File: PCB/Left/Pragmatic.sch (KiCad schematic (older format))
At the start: 75 parts, among them J1 Conn_02x07_Odd_Even, SW1 SW_Push, SW10 SW_Push, SW11 SW_Push, SW12 SW_Push, SW13 SW_Push, SW14 SW_Push, SW15 SW_Push, SW16 SW_Push, SW17 SW_Push, SW18 SW_Push, SW19 SW_Push, SW2 SW_Push, SW20 SW_Push, SW21 SW_Push, SW22 SW_Push, SW23 SW_Push, SW24 SW_Push, SW25 SW_Push, SW26 SW_Push, SW27 SW_Push, SW28 SW_Push, SW29 SW_Push, SW3 SW_Push, SW30 SW_Push, SW31 SW_Push, SW32 SW_Push, SW33 SW_Push, SW34 SW_Push, SW35 SW_Push, SW36 SW_Push, SW4 SW_Push, SW5 SW_Push, SW6 SW_Push, SW7 SW_Push, SW8 SW_Push, SW9 SW_Push

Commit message: left ready
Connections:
- net Col1: now also J1.9 (Pin_9); no longer J1.6 (Pin_6)
- net Col2: now also J1.10 (Pin_10); no longer J1.8 (Pin_8)
- net Col3: now also J1.11 (Pin_11); no longer J1.10 (Pin_10)
- net Col5: now also J1.13 (Pin_13); no longer J1.14 (Pin_14)
- net Col6: now also J1.14 (Pin_14); no longer J1.13 (Pin_13)
- net Row4: now also J1.6 (Pin_6); no longer J1.11 (Pin_11)
- net Row5: now also J1.7 (Pin_7); no longer J1.9 (Pin_9)
- net Row6: now also J1.8 (Pin_8); no longer J1.7 (Pin_7)
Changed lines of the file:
@@
 Text GLabel 6070 2590 2    50   Input ~ 0
 Ground
-Text GLabel 6070 2790 2    50   Input ~ 0
+Text GLabel 5570 2990 0    50   Input ~ 0
 Col1
-Text GLabel 6070 2890 2    50   Input ~ 0
+Text GLabel 6070 2990 2    50   Input ~ 0
 Col2
+Text GLabel 6070 3190 2    50   Input ~ 0
+Col6
 Text GLabel 5570 3190 0    50   Input ~ 0
-Col6
-Text GLabel 6070 3190 2    50   Input ~ 0
 Col5
 Text GLabel 6070 3090 2    50   Input ~ 0
 Col4
-Text GLabel 6070 2990 2    50   Input ~ 0
+Text GLabel 5570 3090 0    50   Input ~ 0
 Col3
-Text GLabel 5570 3090 0    50   Input ~ 0
+Text GLabel 6070 2790 2    50   Input ~ 0
 Row4
-Text GLabel 5570 2990 0    50   Input ~ 0
+Text GLabel 5570 2890 0    50   Input ~ 0
 Row5
-Text GLabel 5570 2890 0    50   Input ~ 0
+Text GLabel 6070 2890 2    50   Input ~ 0
 Row6
 $Comp

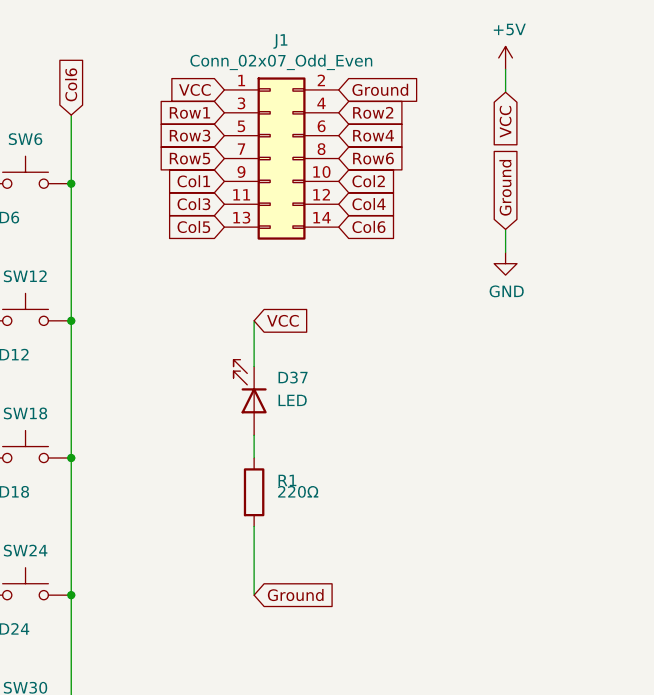
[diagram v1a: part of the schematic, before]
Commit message: fix power track width
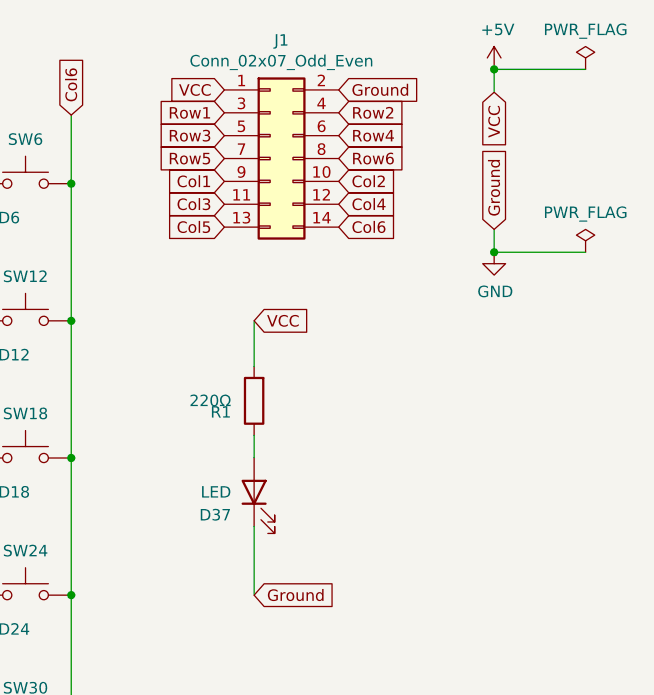
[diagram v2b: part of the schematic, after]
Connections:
- net +5V: now also R1.2; no longer D37.1 (K)
- net GND: now also D37.1 (K); no longer R1.2
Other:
- moved on the sheet: D37, R1
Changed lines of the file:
@@
 Comment4 ""
 $EndDescr
-Text GLabel 6800 3200 1    50   Input ~ 0
+Text GLabel 6750 3200 1    50   Input ~ 0
 Ground
 $Comp
 L power:+5V #PWR01
 U 1 1 6186CA9E
-P 6800 2500
-F 0 "#PWR01" H 6800 2350 50  0001 C CNN
-F 1 "+5V" H 6815 2673 50  0000 C CNN
-F 2 "" H 6800 2500 50  0001 C CNN
-F 3 "" H 6800 2500 50  0001 C CNN
-	1    6800 2500
-	1    0    0    -1
-$EndComp
-Text GLabel 6800 2600 3    50   Input ~ 0
+P 6750 2500
+F 0 "#PWR01" H 6750 2350 50  0001 C CNN
+F 1 "+5V" H 6765 2673 50  0000 C CNN
+F 2 "" H 6750 2500 50  0001 C CNN
+F 3 "" H 6750 2500 50  0001 C CNN
+	1    6750 2500
+	1    0    0    -1
+$EndComp
+Text GLabel 6750 2600 3    50   Input ~ 0
 VCC
 $Comp
 L power:GND #PWR02
 U 1 1 61895032
-P 6800 3300
-F 0 "#PWR02" H 6800 3050 50  0001 C CNN
-F 1 "GND" H 6805 3127 50  0000 C CNN
-F 2 "" H 6800 3300 50  0001 C CNN
-F 3 "" H 6800 3300 50  0001 C CNN
-	1    6800 3300
+P 6750 3300
+F 0 "#PWR02" H 6750 3050 50  0001 C CNN
+F 1 "GND" H 6755 3127 50  0000 C CNN
+F 2 "" H 6750 3300 50  0001 C CNN
+F 3 "" H 6750 3300 50  0001 C CNN
+	1    6750 3300
 	1    0    0    -1
 $EndComp
@@
 L Device:LED D37
 U 1 1 619DFFCE
+P 5700 4350
+F 0 "D37" V 5600 4450 50  0000 L CNN
+F 1 "LED" V 5700 4450 50  0000 L CNN
+F 2 "LED_THT:LED_D3.0mm" H 5700 4350 50  0001 C CNN
+F 3 "~" H 5700 4350 50  0001 C CNN
+	1    5700 4350
+	0    -1   -1   0
+$EndComp
+$Comp
+L Device:R R1
+U 1 1 619DF3E5
 P 5700 3950
-F 0 "D37" V 5600 4050 50  0000 L CNN
-F 1 "LED" V 5700 4050 50  0000 L CNN
-F 2 "LED_THT:LED_D3.0mm" H 5700 3950 50  0001 C CNN
+F 0 "R1" H 5800 4000 50  0000 L CNN
+F 1 "220Ω" H 5800 3950 50  0000 L CNN
+F 2 "Resistor_THT:R_Axial_DIN0207_L6.3mm_D2.5mm_P10.16mm_Horizontal" V 5630 3950 50  0001 C CNN
 F 3 "~" H 5700 3950 50  0001 C CNN
 	1    5700 3950
-	0    1    1    0
-$EndComp
-$Comp
-L Device:R R1
-U 1 1 619DF3E5
-P 5700 4350
-F 0 "R1" H 5800 4400 50  0000 L CNN
-F 1 "220Ω" H 5800 4350 50  0000 L CNN
-F 2 "Resistor_THT:R_Axial_DIN0207_L6.3mm_D2.5mm_P10.16mm_Horizontal" V 5630 4350 50  0001 C CNN
-F 3 "~" H 5700 4350 50  0001 C CNN
-	1    5700 4350
-	1    0    0    -1
+	-1   0    0    1
 $EndComp
 Wire Wire Line
@@
 	5700 4500 5700 4800
 Wire Wire Line
-	6800 2500 6800 2600
-Wire Wire Line
-	6800 3200 6800 3300
-Wire Wire Line
-	5700 4100 5700 4200
+	6750 2500 6750 2600
+Wire Wire Line
+	6750 3200 6750 3300
+Wire Wire Line
+	5700 4200 5700 4100
+$Comp
+L power:PWR_FLAG #FLG0101
+U 1 1 6187BFDE
+P 7150 2500
+F 0 "#FLG0101" H 7150 2575 50  0001 C CNN
+F 1 "PWR_FLAG" H 7150 2673 50  0000 C CNN
+F 2 "" H 7150 2500 50  0001 C CNN
+F 3 "~" H 7150 2500 50  0001 C CNN
+	1    7150 2500
+	1    0    0    -1
+$EndComp
+Wire Wire Line
+	6750 2500 7150 2500
+Connection ~ 6750 2500
+$Comp
+L power:PWR_FLAG #FLG0102
+U 1 1 61881699
+P 7150 3300
+F 0 "#FLG0102" H 7150 3375 50  0001 C CNN
+F 1 "PWR_FLAG" H 7150 3473 50  0000 C CNN
+F 2 "" H 7150 3300 50  0001 C CNN
+F 3 "~" H 7150 3300 50  0001 C CNN
+	1    7150 3300
+	1    0    0    -1
+$EndComp
+Wire Wire Line
+	7150 3300 6750 3300
+Connection ~ 6750 3300
 $EndSCHEMATC

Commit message: double side design
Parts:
- removed J1: Conn_02x07_Odd_Even, Connector_IDC:IDC-Header_2x07_P2.54mm_Vertical, symbol Connector_Generic:Conn_02x07_Odd_Even
- added J1: Conn_02x08_Odd_Even, Connector_IDC:IDC-Header_2x08_P2.54mm_Vertical, symbol Connector_Generic:Conn_02x08_Odd_Even
- added J2: Conn_01x04, kbd:OLED, symbol Connector_Generic:Conn_01x04
- D37: footprint LED_THT:LED_D3.0mm -> LED_SMD:LED_0805_2012Metric_Pad1.15x1.40mm_HandSolder
- R1: footprint Resistor_THT:R_Axial_DIN0207_L6.3mm_D2.5mm_P10.16mm_Horizontal -> Resistor_SMD:R_0805_2012Metric_Pad1.20x1.40mm_HandSolder
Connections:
- net +5V: now also J1.1 (Pin_1), J2.3 (Pin_3)
- net Col1: now also J1.6 (Pin_6)
- net Col2: now also J1.8 (Pin_8)
- net Col3: now also J1.10 (Pin_10)
- net Col4: now also J1.12 (Pin_12)
- net Col5: now also J1.14 (Pin_14)
- net Col6: now also J1.16 (Pin_16)
- net GND: now also J1.2 (Pin_2), J2.4 (Pin_4)
- net Row1: now also J1.5 (Pin_5)
- net Row2: now also J1.7 (Pin_7)
- net Row3: now also J1.9 (Pin_9)
- net Row4: now also J1.11 (Pin_11)
- net Row5: now also J1.13 (Pin_13)
- net Row6: now also J1.15 (Pin_15)
- new net SCL: J1.3 (Pin_3), J2.2 (Pin_2)
- new net SDA: J1.4 (Pin_4), J2.1 (Pin_1)
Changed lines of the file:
@@
 Comment4 ""
 $EndDescr
-Text GLabel 6750 3200 1    50   Input ~ 0
+Text GLabel 10150 3950 1    50   Input ~ 0
 Ground
 $Comp
 L power:+5V #PWR01
 U 1 1 6186CA9E
-P 6750 2500
-F 0 "#PWR01" H 6750 2350 50  0001 C CNN
-F 1 "+5V" H 6765 2673 50  0000 C CNN
-F 2 "" H 6750 2500 50  0001 C CNN
-F 3 "" H 6750 2500 50  0001 C CNN
-	1    6750 2500
-	1    0    0    -1
-$EndComp
-Text GLabel 6750 2600 3    50   Input ~ 0
+P 10150 3250
+F 0 "#PWR01" H 10150 3100 50  0001 C CNN
+F 1 "+5V" H 10165 3423 50  0000 C CNN
+F 2 "" H 10150 3250 50  0001 C CNN
+F 3 "" H 10150 3250 50  0001 C CNN
+	1    10150 3250
+	1    0    0    -1
+$EndComp
+Text GLabel 10150 3350 3    50   Input ~ 0
 VCC
 $Comp
 L power:GND #PWR02
 U 1 1 61895032
-P 6750 3300
-F 0 "#PWR02" H 6750 3050 50  0001 C CNN
-F 1 "GND" H 6755 3127 50  0000 C CNN
-F 2 "" H 6750 3300 50  0001 C CNN
-F 3 "" H 6750 3300 50  0001 C CNN
-	1    6750 3300
+P 10150 4050
+F 0 "#PWR02" H 10150 3800 50  0001 C CNN
+F 1 "GND" H 10155 3877 50  0000 C CNN
+F 2 "" H 10150 4050 50  0001 C CNN
+F 3 "" H 10150 4050 50  0001 C CNN
+	1    10150 4050
 	1    0    0    -1
 $EndComp
@@
 F 0 "D37" V 5600 4450 50  0000 L CNN
 F 1 "LED" V 5700 4450 50  0000 L CNN
-F 2 "LED_THT:LED_D3.0mm" H 5700 4350 50  0001 C CNN
+F 2 "LED_SMD:LED_0805_2012Metric_Pad1.15x1.40mm_HandSolder" H 5700 4350 50  0001 C CNN
 F 3 "~" H 5700 4350 50  0001 C CNN
 	1    5700 4350
@@
 F 0 "R1" H 5800 4000 50  0000 L CNN
 F 1 "220Ω" H 5800 3950 50  0000 L CNN
-F 2 "Resistor_THT:R_Axial_DIN0207_L6.3mm_D2.5mm_P10.16mm_Horizontal" V 5630 3950 50  0001 C CNN
+F 2 "Resistor_SMD:R_0805_2012Metric_Pad1.20x1.40mm_HandSolder" V 5630 3950 50  0001 C CNN
 F 3 "~" H 5700 3950 50  0001 C CNN
 	1    5700 3950
@@
 	0    -1   -1   0
 $EndComp
-$Comp
-L Connector_Generic:Conn_02x07_Odd_Even J1
-U 1 1 61867C1C
-P 5770 2890
-F 0 "J1" H 5820 3407 50  0000 C CNN
-F 1 "Conn_02x07_Odd_Even" H 5820 3316 50  0000 C CNN
-F 2 "Connector_IDC:IDC-Header_2x07_P2.54mm_Vertical" H 5770 2890 50  0001 C CNN
-F 3 "~" H 5770 2890 50  0001 C CNN
-	1    5770 2890
-	1    0    0    -1
-$EndComp
-Text GLabel 5570 2590 0    50   Input ~ 0
-VCC
-Text GLabel 5570 2690 0    50   Input ~ 0
-Row1
-Text GLabel 6070 2690 2    50   Input ~ 0
-Row2
-Text GLabel 5570 2790 0    50   Input ~ 0
-Row3
-Text GLabel 6070 2590 2    50   Input ~ 0
-Ground
-Text GLabel 5570 2990 0    50   Input ~ 0
-Col1
-Text GLabel 6070 2990 2    50   Input ~ 0
-Col2
-Text GLabel 6070 3190 2    50   Input ~ 0
-Col6
-Text GLabel 5570 3190 0    50   Input ~ 0
-Col5
-Text GLabel 6070 3090 2    50   Input ~ 0
-Col4
-Text GLabel 5570 3090 0    50   Input ~ 0
-Col3
-Text GLabel 6070 2790 2    50   Input ~ 0
-Row4
-Text GLabel 5570 2890 0    50   Input ~ 0
-Row5
-Text GLabel 6070 2890 2    50   Input ~ 0
-Row6
 $Comp
 L Switch:SW_Push SW8
@@
 	5700 4500 5700 4800
 Wire Wire Line
-	6750 2500 6750 2600
-Wire Wire Line
-	6750 3200 6750 3300
+	10150 3250 10150 3350
+Wire Wire Line
+	10150 3950 10150 4050
 Wire Wire Line
 	5700 4200 5700 4100
@@
 L power:PWR_FLAG #FLG0101
 U 1 1 6187BFDE
-P 7150 2500
-F 0 "#FLG0101" H 7150 2575 50  0001 C CNN
-F 1 "PWR_FLAG" H 7150 2673 50  0000 C CNN
-F 2 "" H 7150 2500 50  0001 C CNN
-F 3 "~" H 7150 2500 50  0001 C CNN
-	1    7150 2500
-	1    0    0    -1
-$EndComp
-Wire Wire Line
-	6750 2500 7150 2500
-Connection ~ 6750 2500
+P 10550 3250
+F 0 "#FLG0101" H 10550 3325 50  0001 C CNN
+F 1 "PWR_FLAG" H 10550 3423 50  0000 C CNN
+F 2 "" H 10550 3250 50  0001 C CNN
+F 3 "~" H 10550 3250 50  0001 C CNN
+	1    10550 3250
+	1    0    0    -1
+$EndComp
+Wire Wire Line
+	10150 3250 10550 3250
+Connection ~ 10150 3250
 $Comp
 L power:PWR_FLAG #FLG0102
 U 1 1 61881699
-P 7150 3300
-F 0 "#FLG0102" H 7150 3375 50  0001 C CNN
-F 1 "PWR_FLAG" H 7150 3473 50  0000 C CNN
-F 2 "" H 7150 3300 50  0001 C CNN
-F 3 "~" H 7150 3300 50  0001 C CNN
-	1    7150 3300
-	1    0    0    -1
-$EndComp
-Wire Wire Line
-	7150 3300 6750 3300
-Connection ~ 6750 3300
+P 10550 4050
+F 0 "#FLG0102" H 10550 4125 50  0001 C CNN
+F 1 "PWR_FLAG" H 10550 4223 50  0000 C CNN
+F 2 "" H 10550 4050 50  0001 C CNN
+F 3 "~" H 10550 4050 50  0001 C CNN
+	1    10550 4050
+	1    0    0    -1
+$EndComp
+Wire Wire Line
+	10550 4050 10150 4050
+Connection ~ 10150 4050
+$Comp
+L Connector_Generic:Conn_02x08_Odd_Even J1
+U 1 1 6194905D
+P 5950 2850
+F 0 "J1" H 6000 3367 50  0000 C CNN
+F 1 "Conn_02x08_Odd_Even" H 6000 3276 50  0000 C CNN
+F 2 "Connector_IDC:IDC-Header_2x08_P2.54mm_Vertical" H 5950 2850 50  0001 C CNN
+F 3 "~" H 5950 2850 50  0001 C CNN
+	1    5950 2850
+	1    0    0    -1
+$EndComp
+Text GLabel 5750 2550 0    50   Input ~ 0
+VCC
+Text GLabel 6250 2550 2    50   Input ~ 0
+GND
+Text GLabel 6250 2650 2    50   Input ~ 0
+SDA
+Text GLabel 5750 2650 0    50   Input ~ 0
+SCL
+Text GLabel 5750 2750 0    50   Input ~ 0
+Row1
+Text GLabel 5750 2850 0    50   Input ~ 0
+Row2
+Text GLabel 5750 2950 0    50   Input ~ 0
+Row3
+Text GLabel 5750 3050 0    50   Input ~ 0
+Row4
+Text GLabel 5750 3150 0    50   Input ~ 0
+Row5
+Text GLabel 5750 3250 0    50   Input ~ 0
+Row6
+Text GLabel 6250 2750 2    50   Input ~ 0
+Col1
+Text GLabel 6250 2850 2    50   Input ~ 0
+Col2
+Text GLabel 6250 2950 2    50   Input ~ 0
+Col3
+Text GLabel 6250 3050 2    50   Input ~ 0
+Col4
+Text GLabel 6250 3150 2    50   Input ~ 0
+Col5
+Text GLabel 6250 3250 2    50   Input ~ 0
+Col6
+$Comp
+L Connector_Generic:Conn_01x04 J2
+U 1 1 6195FBC7
+P 7100 2750
+F 0 "J2" H 7018 2325 50  0000 C CNN
+F 1 "Conn_01x04" H 7018 2416 50  0000 C CNN
+F 2 "kbd:OLED" H 7100 2750 50  0001 C CNN
+F 3 "~" H 7100 2750 50  0001 C CNN
+	1    7100 2750
+	-1   0    0    1
+$EndComp
+Text GLabel 7300 2550 2    50   Input ~ 0
+GND
+Text GLabel 7300 2750 2    50   Input ~ 0
+SCL
+Text GLabel 7300 2850 2    50   Input ~ 0
+SDA
+Text GLabel 7300 2650 2    50   Input ~ 0
+VCC
 $EndSCHEMATC
